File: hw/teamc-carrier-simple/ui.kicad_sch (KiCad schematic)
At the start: 14 parts, among them J10 GO/STOP button, J11 role toggle, J12 mode toggle, J14 LED lead

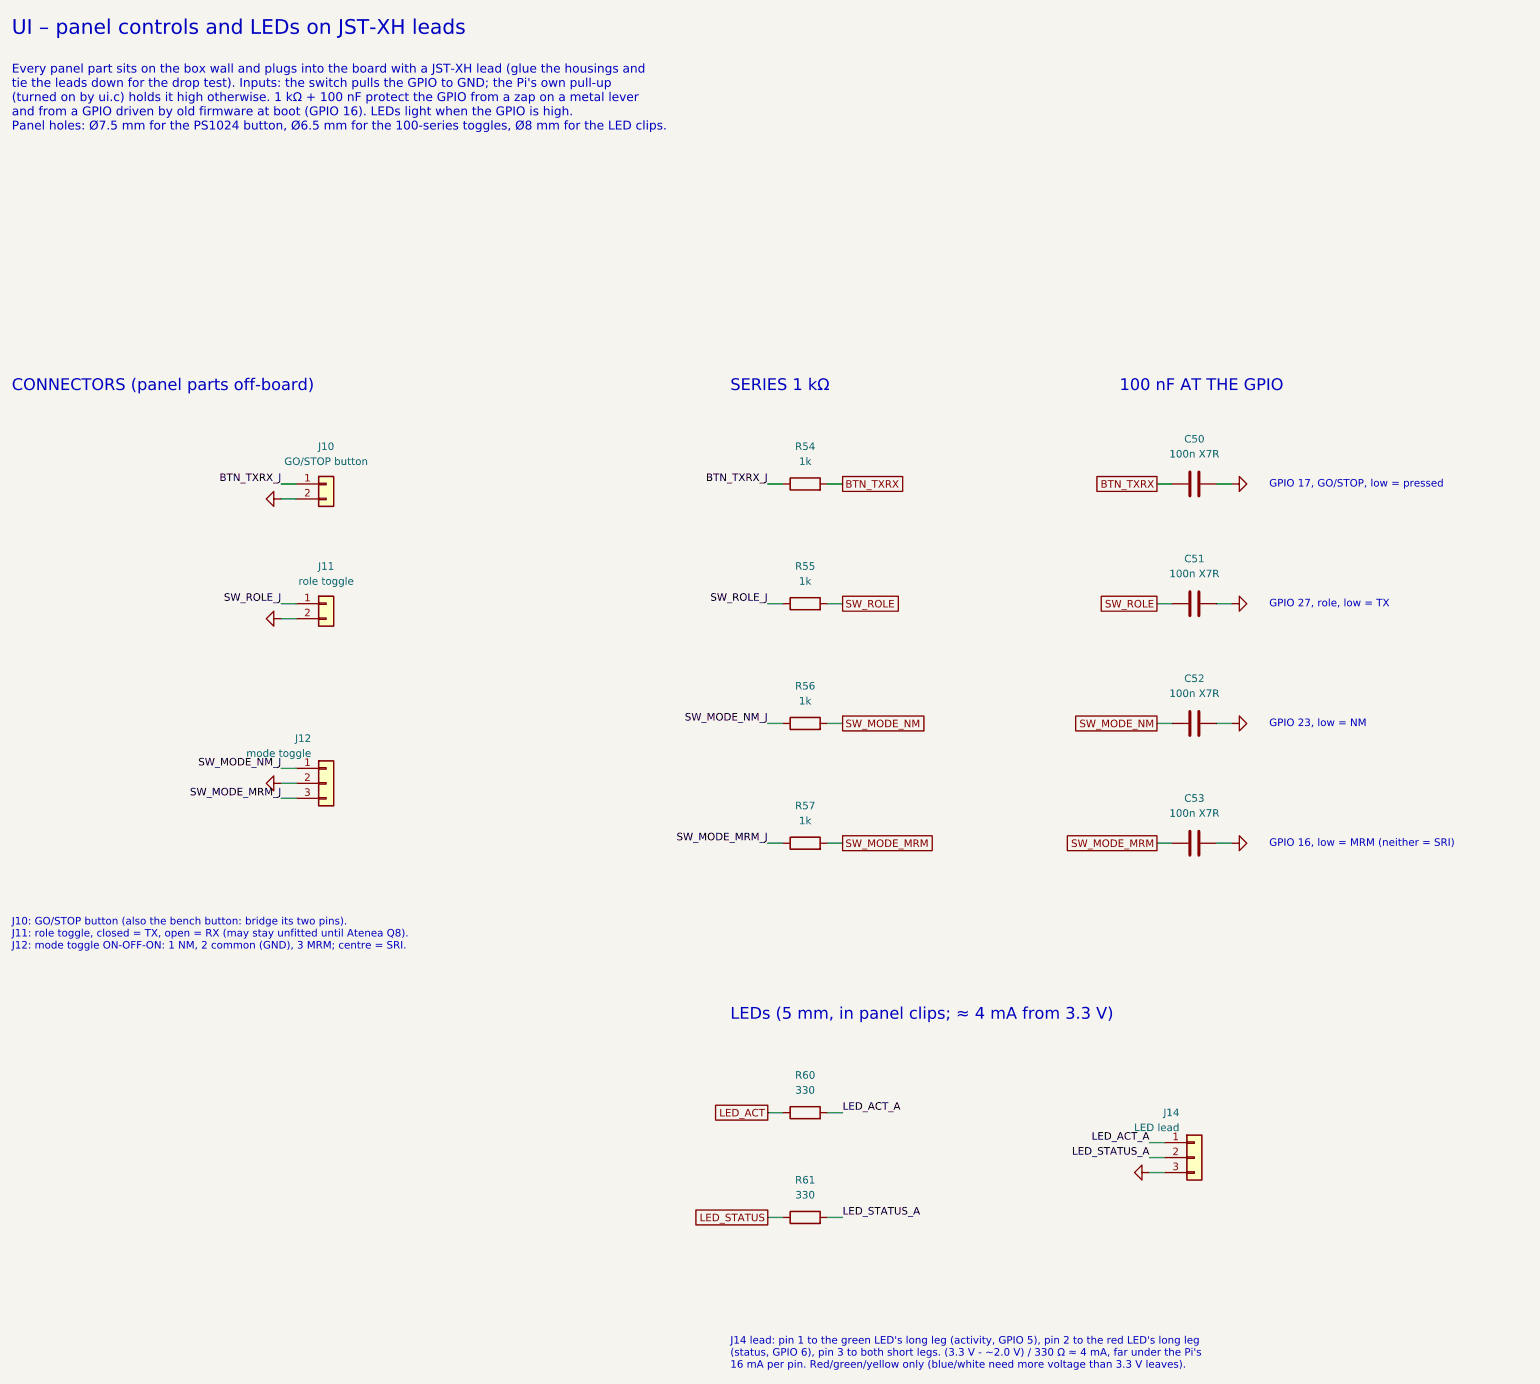
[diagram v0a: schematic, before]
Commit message: Carrier rev C (simple): checkpoint 3 - placed and routed on one copper layer, DRC 0/0/0, 4 wire links
120 x 66 mm (box not measured yet: hw/scripts/layout_carrier_simple.py rebuilds everything after the
outline in place_carrier_simple.py changes). Backbone hand-routed (route_carrier_simple.py), router for
the short branches, GND pour; DRC with schematic parity 0 violations / 0 unconnected / 0 parity, all
severities; ERC 0/0. Tracks 0.8-2.0 mm. Wire links: IRQ over CSN and three ground pockets. Crossings by
tracks between resistor legs (SCK under R84/R83, LED_ACT_A under R61, CSN/IRQ under R57).
Layout-driven schematic changes: input 100 nF caps dropped, C18 at the toggle lead, 7.62 mm resistor
pitch, D1 on 12.7 mm, three M3 holes. Cable-tie slot + edge notch at the cell. 3D models for the
modules, wire links, holder, fuse clips and test points (gen_3d_revc.py; fetch_3d substitutes).
Fab: F.Cu + Edge.Cuts gerbers, drill, 1:1 copper PDFs, assembly PDFs, wire_links.csv, zip; renders.

Co-Authored-By: Claude Opus 5.5 <noreply@anthropic.com>
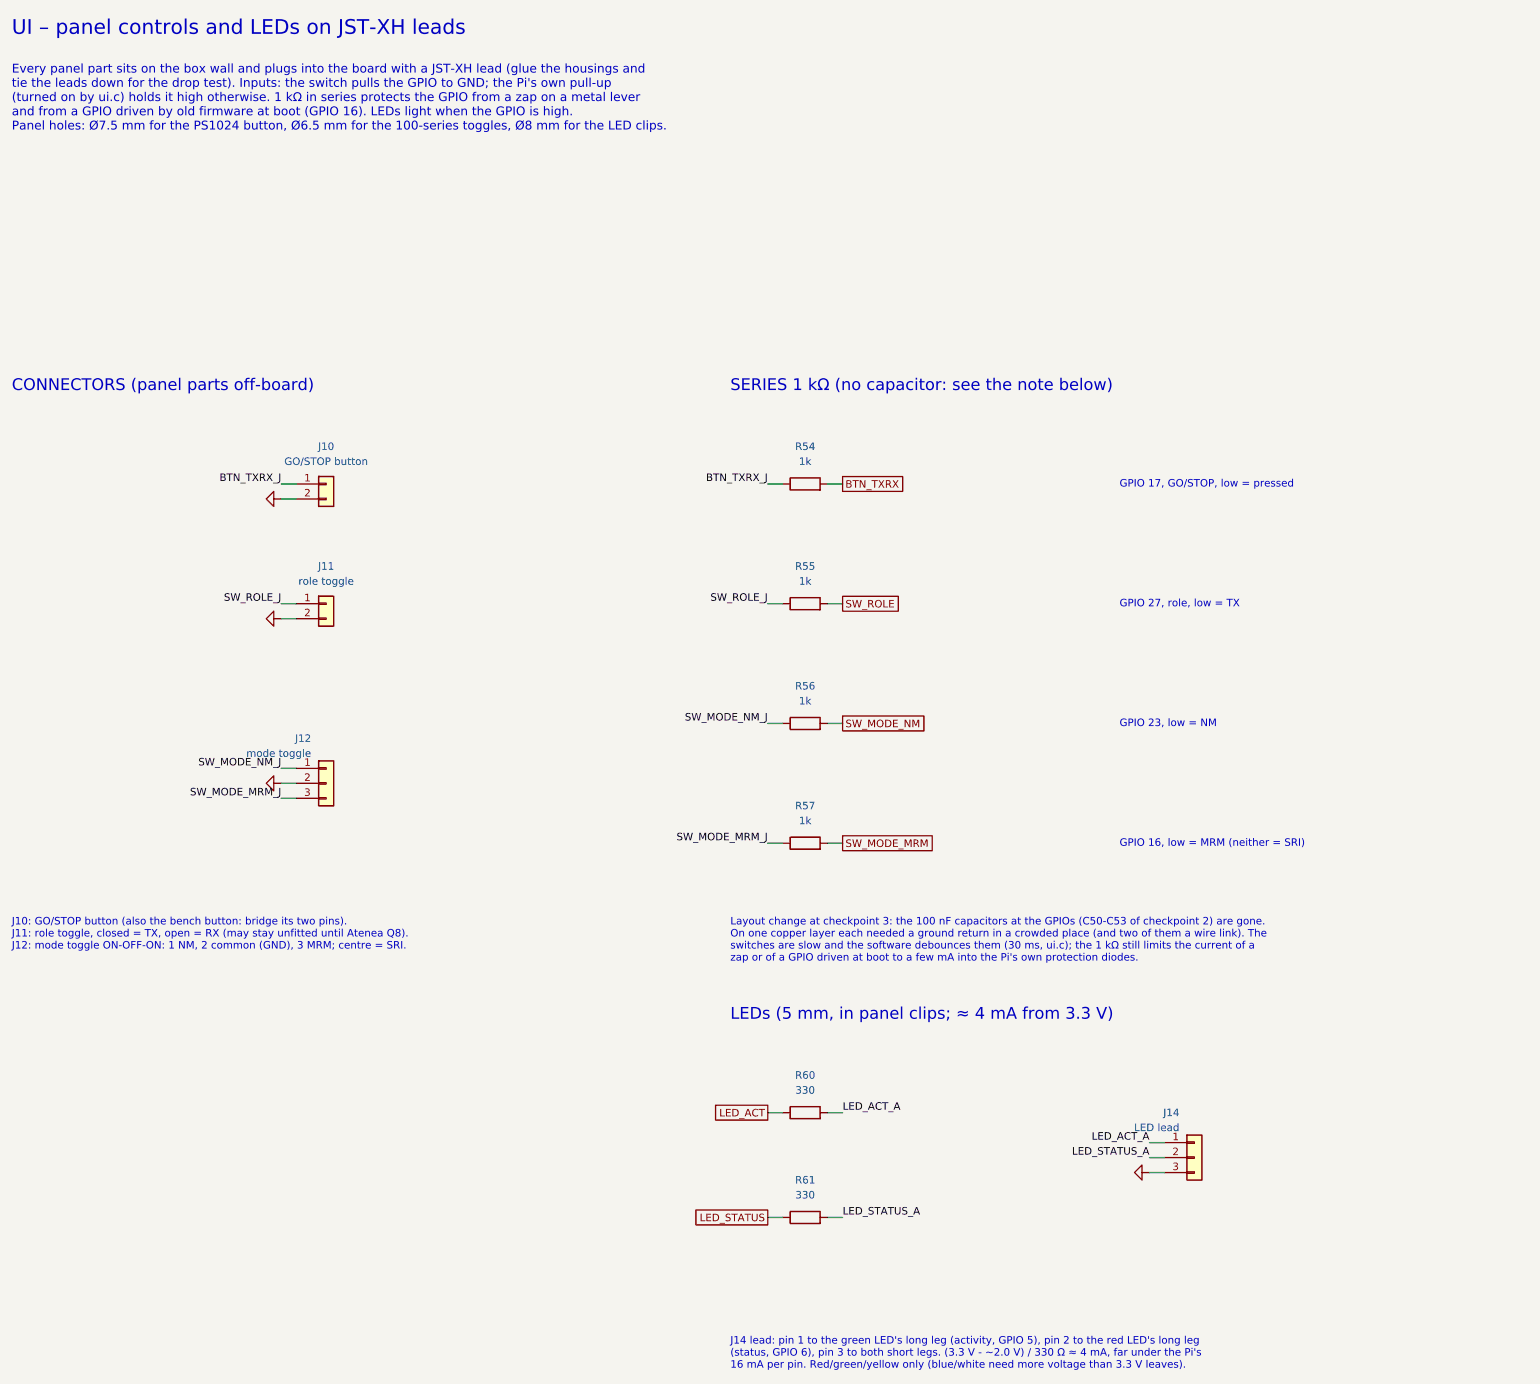
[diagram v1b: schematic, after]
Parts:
- removed C50, C51, C52, C53: 100n X7R, teamc:C_Disc_D5.0mm_W2.5mm_P5.00mm_Pad1.8mm, symbol Device:C
- R54, R55, R56, R57, R60, R61: footprint teamc:R_Axial_DIN0207_L6.3mm_D2.5mm_P10.16mm_Horizontal_Pad1.8mm -> teamc:R_Axial_DIN0207_L6.3mm_D2.5mm_P7.62mm_Horizontal_Pad1.8mm
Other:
- note added: "Every panel part sits on the box wall and plugs into the board with a JST-XH lead (glue the housings and tie the leads down for the drop test). Inputs: the switch pulls the GPIO to GND; the Pi's own pull-up (turned on by ui.c) holds it high otherwise. 1 kΩ in series protects the GPIO from a zap on a metal lever and from a GPIO driven by old firmware at boot (GPIO 16). LEDs light when the GPIO is 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"
- note added: "Layout change at checkpoint 3: the 100 nF capacitors at the GPIOs (C50-C53 of checkpoint 2) are gone. On one copper layer each needed a ground return in a crowded place (and two of them a wire link). The switches are slow and the software debounces them (30 ms, ui.c); the 1 kΩ still limits the current of a zap or of a GPIO driven at boot to a few mA into the Pi's own protection diodes."
- note added: "SERIES 1 kΩ (no capacitor: see the note below)"
- note removed: "100 nF AT THE GPIO"
- note removed: "Every panel part sits on the box wall and plugs into the board with a JST-XH lead (glue the housings and tie the leads down for the drop test). Inputs: the switch pulls the GPIO to GND; the Pi's own pull-up (turned on by ui.c) holds it high otherwise. 1 kΩ + 100 nF protect the GPIO from a zap on a metal lever and from a GPIO driven by old firmware at boot (GPIO 16). LEDs light when the GPIO is hi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"
- note removed: "SERIES 1 kΩ"

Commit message: Carrier rev C (simple): checkpoint-3 fixes (P4KE10A TVS per panel lead, wire-loop test points), board 120 x 68 mm, build guide and shopping list
- D12-D16 P4KE10A (DO-41 standing) at the panel-lead connectors; TP2/TP3/TP4 low wire loops (TP2/TP4 under the breakout)
- J13 UART order kept as rev A/B (1 GND, 2 TX, 3 RX); ui.py docstring fixed
- layout: TVS rows, R56/CSN lowered, board 66 -> 68 mm so the GND pour keeps a >= 1.9 mm channel between its halves
- own 3D stand-in for the 3.81 mm vertical DO-41 (none upstream); ERC 0/0, DRC 0/0/0, 4 wire links, renders resolved
- hw/REVC_GUIDE.md, hw/REVC_SHOPPING.md, DESIGN_NOTES rev C section, BoM EUR 145.51/box; reviewer fixes in the guide

Co-Authored-By: Claude Opus 5.5 <noreply@anthropic.com>
Claude-Session: https://claude.ai/code/session_01PKzvcoWGaf5niy6TrXYsya
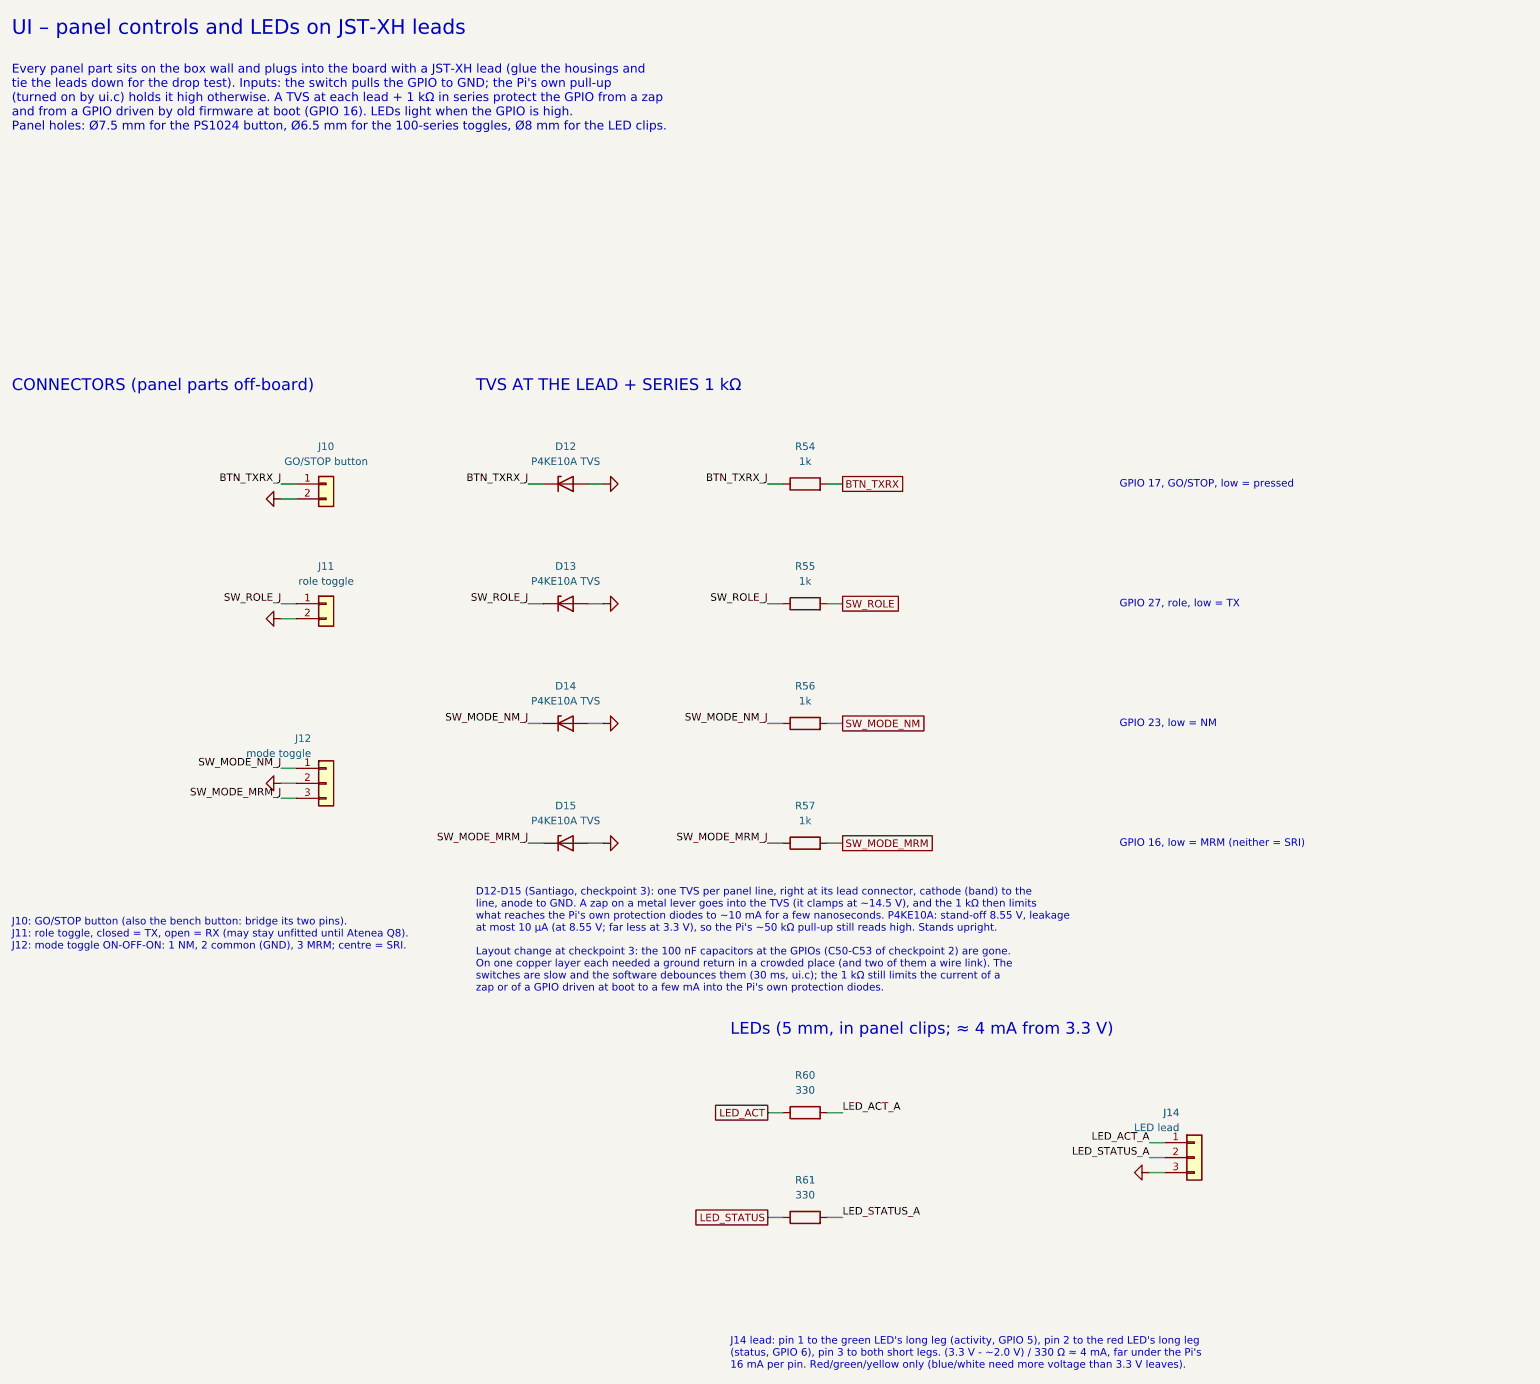
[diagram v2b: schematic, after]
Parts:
- added D12, D13, D14, D15: P4KE10A TVS, Diode_THT:D_DO-41_SOD81_P3.81mm_Vertical_CathodeUp, symbol Device:D_Zener
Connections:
- net BTN_TXRX_J: now also D12.1 (K)
- net GND: now also D12.2 (A), D13.2 (A), D14.2 (A), D15.2 (A)
- net SW_MODE_MRM_J: now also D15.1 (K)
- net SW_MODE_NM_J: now also D14.1 (K)
- net SW_ROLE_J: now also D13.1 (K)
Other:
- note added: "D12-D15 (Santiago, checkpoint 3): one TVS per panel line, right at its lead connector, cathode (band) to the line, anode to GND. A zap on a metal lever goes into the TVS (it clamps at ~14.5 V), and the 1 kΩ then limits what reaches the Pi's own protection diodes to ~10 mA for a few nanoseconds. P4KE10A: stand-off 8.55 V, leakage at most 10 µA (at 8.55 V; far less at 3.3 V), so the Pi's ~50 kΩ pul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"
- note added: "Every panel part sits on the box wall and plugs into the board with a JST-XH lead (glue the housings and tie the leads down for the drop test). Inputs: the switch pulls the GPIO to GND; the Pi's own pull-up (turned on by ui.c) holds it high otherwise. A TVS at each lead + 1 kΩ in series protect the GPIO from a zap and from a GPIO driven by old firmware at boot (GPIO 16). LEDs light when the GPIO 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"
- note added: "TVS AT THE LEAD + SERIES 1 kΩ"
- note removed: "Every panel part sits on the box wall and plugs into the board with a JST-XH lead (glue the housings and tie the leads down for the drop test). Inputs: the switch pulls the GPIO to GND; the Pi's own pull-up (turned on by ui.c) holds it high otherwise. 1 kΩ in series protects the GPIO from a zap on a metal lever and from a GPIO driven by old firmware at boot (GPIO 16). LEDs light when the GPIO is 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"
- note removed: "SERIES 1 kΩ (no capacitor: see the note below)"
